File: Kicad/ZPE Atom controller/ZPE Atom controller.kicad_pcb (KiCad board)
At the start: 2 copper layers, 160 x 71.1 mm, 31 parts, among them IC1 TC4424AVPA, P1 CONN_01X18, P2 CONN_01X18, Q1 PN2222A, T1 Transformer_SP_1S, U1 SSD1306

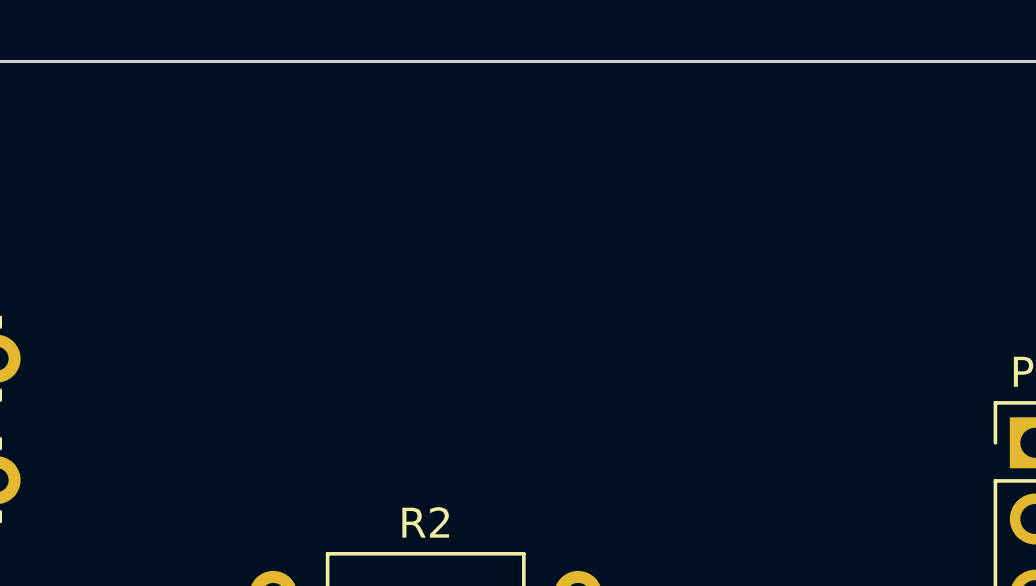
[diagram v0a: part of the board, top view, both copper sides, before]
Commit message: Updated footprint cd4049
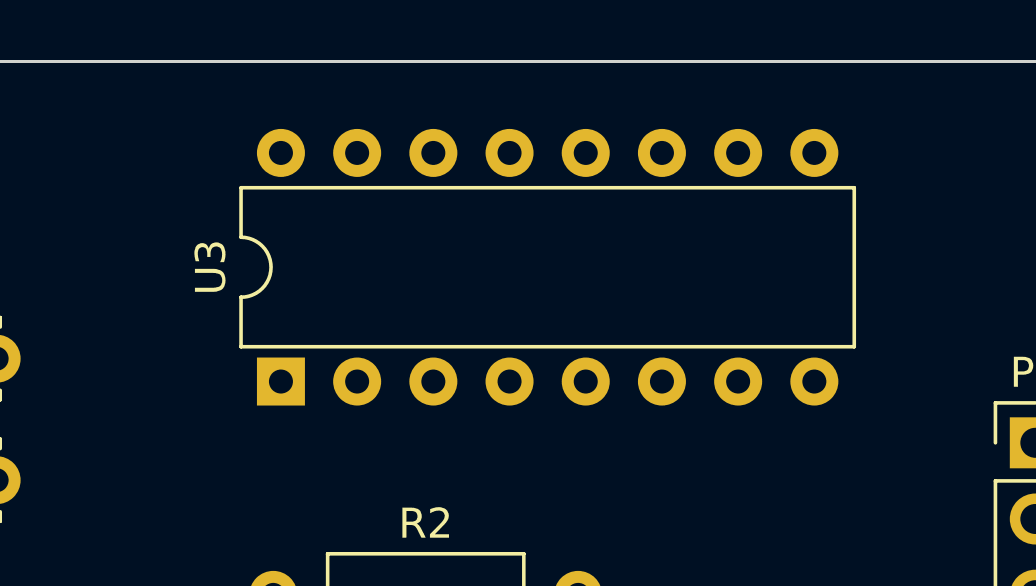
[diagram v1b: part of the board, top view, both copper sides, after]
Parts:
- added U3: 4049, Package_DIP:DIP-16_W7.62mm, F.Cu at (152.7, 71.6)
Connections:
- IC1 pad 4: unconnected-(IC1-IN_B) -> Net-(IC1-IN_B)

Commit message: Updated board inverter
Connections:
- U3 pad 1: (no net) -> +3V3
- U3 pad 16: (no net) -> +3V3
- U3 pad 8: (no net) -> GND
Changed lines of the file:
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@@
     (fp_line (start 6.985 19.05) (end 0.635 19.05)
       (stroke (width 0.1) (type solid)) (layer "F.Fab"))
-    (pad "1" thru_hole rect (at 0 0 90) (size 1.6 1.6) (drill 0.8) (layers *.Cu *.Mask))
+    (pad "1" thru_hole rect (at 0 0 90) (size 1.6 1.6) (drill 0.8) (layers *.Cu *.Mask)
+      (net 10 "+3V3") (pinfunction "VDD") (pintype "power_in"))
     (pad "2" thru_hole oval (at 0 2.54 90) (size 1.6 1.6) (drill 0.8) (layers *.Cu *.Mask)
       (net 44 "Net-(IC1-IN_B)") (pintype "output"))
@@
     (pad "6" thru_hole oval (at 0 12.7 90) (size 1.6 1.6) (drill 0.8) (layers *.Cu *.Mask))
     (pad "7" thru_hole oval (at 0 15.24 90) (size 1.6 1.6) (drill 0.8) (layers *.Cu *.Mask))
-    (pad "8" thru_hole oval (at 0 17.78 90) (size 1.6 1.6) (drill 0.8) (layers *.Cu *.Mask))
+    (pad "8" thru_hole oval (at 0 17.78 90) (size 1.6 1.6) (drill 0.8) (layers *.Cu *.Mask)
+      (net 6 "GND") (pinfunction "GND") (pintype "power_in"))
     (pad "9" thru_hole oval (at 7.62 17.78 90) (size 1.6 1.6) (drill 0.8) (layers *.Cu *.Mask))
     (pad "10" thru_hole oval (at 7.62 15.24 90) (size 1.6 1.6) (drill 0.8) (layers *.Cu *.Mask))
@@
     (pad "14" thru_hole oval (at 7.62 5.08 90) (size 1.6 1.6) (drill 0.8) (layers *.Cu *.Mask))
     (pad "15" thru_hole oval (at 7.62 2.54 90) (size 1.6 1.6) (drill 0.8) (layers *.Cu *.Mask))
-    (pad "16" thru_hole oval (at 7.62 0 90) (size 1.6 1.6) (drill 0.8) (layers *.Cu *.Mask))
+    (pad "16" thru_hole oval (at 7.62 0 90) (size 1.6 1.6) (drill 0.8) (layers *.Cu *.Mask)
+      (net 10 "+3V3") (pinfunction "VCC") (pintype "power_in"))
     (model "${KICAD6_3DMODEL_DIR}/Package_DIP.3dshapes/DIP-16_W7.62mm.wrl"
       (offset (xyz 0 0 0))
